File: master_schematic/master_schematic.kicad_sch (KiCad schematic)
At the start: 5 parts, among them U1 teensy_4.1

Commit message: added footprint library and a pcb file
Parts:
- removed U2: ~, symbol hb_symbol_lib:load_cell_yzc516_50kg
- added U3: ~, symbol hb_symbol_lib:new_load_cell_gx-1
- PT1: footprint (none) -> hb_footprint_lib:Pressure Transducer (Low)
- RM1: footprint (none) -> hb_footprint_lib:Radio_Module
- U1: footprint DEV-16771:MODULE_DEV-16771 -> hb_footprint_lib:teensy4.1
- U4: footprint (none) -> Connector_PinHeader_1.00mm:PinHeader_1x06_P1.00mm_Vertical
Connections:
- net LC_SIG+: now also U4.9 (A+), U3.2 (SIG+)
- net LC_SIG-: now also U4.8 (A-), U3.3 (SIG-)
- net LC_VDD: now reaches U4.12 (E+)
- net LC_VDD: now also U3.1 (VDD)
- net LC_GND: now reaches U4.7 (E-)
- net LC_GND: now also U3.4 (GND)
- net PT_INPUT renamed PT_OUTPUT
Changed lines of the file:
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@@
+	(wire
+		(pts
+			(xy 45.72 123.19) (xy 45.72 125.73)
+		)
+		(stroke
+			(width 0)
+			(type default)
+		)
+	)
 	(wire
 		(pts
@@
 	(wire
 		(pts
+			(xy 48.26 99.06) (xy 53.34 99.06)
+		)
+		(stroke
+			(width 0)
+			(type default)
+		)
+	)
+	(wire
+		(pts
 			(xy 168.91 73.66) (xy 175.26 73.66)
 		)
@@
 	(wire
 		(pts
+			(xy 50.8 123.19) (xy 50.8 125.73)
+		)
+		(stroke
+			(width 0)
+			(type default)
+		)
+	)
+	(wire
+		(pts
 			(xy 128.27 46.99) (xy 137.16 46.99)
 		)
@@
 	(wire
 		(pts
-			(xy 48.26 86.36) (xy 53.34 86.36)
+			(xy 48.26 123.19) (xy 48.26 125.73)
 		)
 		(stroke
@@
 	(wire
 		(pts
+			(xy 48.26 104.14) (xy 53.34 104.14)
+		)
+		(stroke
+			(width 0)
+			(type default)
+		)
+	)
+	(wire
+		(pts
 			(xy 80.01 82.55) (xy 87.63 82.55)
 		)
@@
 	(wire
 		(pts
-			(xy 48.26 88.9) (xy 53.34 88.9)
-		)
-		(stroke
-			(width 0)
-			(type default)
-		)
-	)
-	(wire
-		(pts
 			(xy 168.91 55.88) (xy 175.26 55.88)
 		)
@@
 	(wire
 		(pts
+			(xy 48.26 106.68) (xy 53.34 106.68)
+		)
+		(stroke
+			(width 0)
+			(type default)
+		)
+	)
+	(wire
+		(pts
 			(xy 168.91 71.12) (xy 175.26 71.12)
 		)
@@
 	(wire
 		(pts
+			(xy 58.42 123.19) (xy 58.42 125.73)
+		)
+		(stroke
+			(width 0)
+			(type default)
+		)
+	)
+	(wire
+		(pts
 			(xy 45.72 151.13) (xy 45.72 157.48)
 		)
@@
 	(wire
 		(pts
-			(xy 48.26 78.74) (xy 53.34 78.74)
-		)
-		(stroke
-			(width 0)
-			(type default)
-		)
-	)
-	(wire
-		(pts
 			(xy 128.27 140.97) (xy 135.89 140.97)
 		)
@@
 	(wire
 		(pts
-			(xy 48.26 81.28) (xy 53.34 81.28)
-		)
-		(stroke
-			(width 0)
-			(type default)
-		)
-	)
-	(wire
-		(pts
 			(xy 55.88 151.13) (xy 55.88 157.48)
 		)
@@
 		)
 	)
-	(label "LC_SIG+"
-		(at 53.34 81.28 0)
+	(wire
+		(pts
+			(xy 48.26 101.6) (xy 53.34 101.6)
+		)
+		(stroke
+			(width 0)
+			(type default)
+		)
+	)
+	(label "LC_SIG-"
+		(at 53.34 104.14 0)
 		(fields_autoplaced yes)
 		(effects
@@
 		)
 	)
+	(label "LC_SIG+"
+		(at 53.34 101.6 0)
+		(fields_autoplaced yes)
+		(effects
+			(font
+				(size 1.27 1.27)
+			)
+			(justify left bottom)
+		)
+	)
 	(label "AMP_DATA"
 		(at 55.88 157.48 270)
@@
 		)
 	)
+	(label "LC_SIG+"
+		(at 50.8 123.19 90)
+		(fields_autoplaced yes)
+		(effects
+			(font
+				(size 1.27 1.27)
+			)
+			(justify left bottom)
+		)
+	)
 	(label "CS4RM"
 		(at 168.91 73.66 180)
@@
 		)
 	)
-	(label "GND"
-		(at 53.34 88.9 0)
-		(fields_autoplaced yes)
-		(effects
-			(font
-				(size 1.27 1.27)
-			)
-			(justify left bottom)
-		)
-	)
-	(label "PT_INPUT"
+	(label "LC_GND"
+		(at 45.72 123.19 90)
+		(fields_autoplaced yes)
+		(effects
+			(font
+				(size 1.27 1.27)
+			)
+			(justify left bottom)
+		)
+	)
+	(label "PT_OUTPUT"
 		(at 80.01 115.57 180)
 		(fields_autoplaced yes)
@@
 			)
 			(justify right bottom)
-		)
-	)
-	(label "LC_SIG-"
-		(at 53.34 86.36 0)
-		(fields_autoplaced yes)
-		(effects
-			(font
-				(size 1.27 1.27)
-			)
-			(justify left bottom)
 		)
 	)
@@
 		)
 	)
+	(label "LC_VDD"
+		(at 58.42 123.19 90)
+		(fields_autoplaced yes)
+		(effects
+			(font
+				(size 1.27 1.27)
+			)
+			(justify left bottom)
+		)
+	)
 	(label "GND"
 		(at 168.91 58.42 180)
@@
 		)
 	)
+	(label "LC_VDD"
+		(at 53.34 99.06 0)
+		(fields_autoplaced yes)
+		(effects
+			(font
+				(size 1.27 1.27)
+			)
+			(justify left bottom)
+		)
+	)
 	(label "SCK"
 		(at 168.91 66.04 180)
@@
 		)
 	)
-	(label "5V"
-		(at 53.34 78.74 0)
-		(fields_autoplaced yes)
-		(effects
-			(font
-				(size 1.27 1.27)
-			)
-			(justify left bottom)
-		)
-	)
 	(label "RST4RM"
 		(at 168.91 76.2 180)
@@
 		)
 	)
+	(label "LC_GND"
+		(at 53.34 106.68 0)
+		(fields_autoplaced yes)
+		(effects
+			(font
+				(size 1.27 1.27)
+			)
+			(justify left bottom)
+		)
+	)
 	(label "IRQ4RM"
 		(at 80.01 74.93 180)
@@
 		)
 	)
-	(label "PT_INPUT"
+	(label "PT_OUTPUT"
 		(at 198.12 99.06 0)
+		(fields_autoplaced yes)
+		(effects
+			(font
+				(size 1.27 1.27)
+			)
+			(justify left bottom)
+		)
+	)
+	(label "LC_SIG-"
+		(at 48.26 123.19 90)
 		(fields_autoplaced yes)
 		(effects
@@
 			)
 		)
-		(property "Footprint" "DEV-16771:MODULE_DEV-16771"
+		(property "Footprint" "hb_footprint_lib:teensy4.1"
 			(at 108.458 163.576 0)
 			(effects
@@
 				(path "/c4f7e98c-e88d-49cc-9841-b70710a90a72"
 					(reference "U1")
+					(unit 1)
+				)
+			)
+		)
+	)
+	(symbol
+		(lib_id "hb_symbol_lib:new_load_cell_gx-1")
+		(at 40.64 102.87 0)
+		(unit 1)
+		(exclude_from_sim no)
+		(in_bom yes)
+		(on_board yes)
+		(dnp no)
+		(fields_autoplaced yes)
+		(property "Reference" "U3"
+			(at 40.005 93.98 0)
+			(effects
+				(font
+					(size 1.27 1.27)
+				)
+			)
+		)
+		(property "Value" "~"
+			(at 40.005 96.52 0)
+			(effects
+				(font
+					(size 1.27 1.27)
+				)
+			)
+		)
+		(property "Footprint" ""
+			(at 38.1 102.616 0)
+			(effects
+				(font
+					(size 1.27 1.27)
+				)
+				(hide yes)
+			)
+		)
+		(property "Datasheet" ""
+			(at 38.1 102.616 0)
+			(effects
+				(font
+					(size 1.27 1.27)
+				)
+				(hide yes)
+			)
+		)
+		(property "Description" ""
+			(at 38.1 102.616 0)
+			(effects
+				(font
+					(size 1.27 1.27)
+				)
+				(hide yes)
+			)
+		)
+		(pin "1"
+		)
+		(pin "2"
+		)
+		(pin "3"
+		)
+		(pin "4"
+		)
+		(instances
+			(project ""
+				(path "/c4f7e98c-e88d-49cc-9841-b70710a90a72"
+					(reference "U3")
 					(unit 1)
 				)
@@
 			)
 		)
-		(property "Footprint" ""
+		(property "Footprint" "hb_footprint_lib:Radio_Module"
 			(at 195.58 52.07 0)
 			(effects
@@
 			)
 		)
-		(property "Footprint" ""
+		(property "Footprint" "hb_footprint_lib:Pressure Transducer (Low)"
 			(at 184.15 101.6 0)
 			(effects
@@
 				(path "/c4f7e98c-e88d-49cc-9841-b70710a90a72"
 					(reference "PT1")
-					(unit 1)
-				)
-			)
-		)
-	)
-	(symbol
-		(lib_id "hb_symbol_lib:load_cell_yzc516_50kg")
-		(at 38.1 82.55 0)
-		(unit 1)
-		(exclude_from_sim no)
-		(in_bom yes)
-		(on_board yes)
-		(dnp no)
-		(fields_autoplaced yes)
-		(property "Reference" "U2"
-			(at 38.735 73.66 0)
-			(effects
-				(font
-					(size 1.27 1.27)
-				)
-			)
-		)
-		(property "Value" "~"
-			(at 38.735 76.2 0)
-			(effects
-				(font
-					(size 1.27 1.27)
-				)
-			)
-		)
-		(property "Footprint" ""
-			(at 38.1 82.55 0)
-			(effects
-				(font
-					(size 1.27 1.27)
-				)
-				(hide yes)
-			)
-		)
-		(property "Datasheet" ""
-			(at 38.1 82.55 0)
-			(effects
-				(font
-					(size 1.27 1.27)
-				)
-				(hide yes)
-			)
-		)
-		(property "Description" ""
-			(at 38.1 82.55 0)
-			(effects
-				(font
-					(size 1.27 1.27)
-				)
-				(hide yes)
-			)
-		)
-		(pin "5"
-		)
-		(pin "1"
-		)
-		(pin "3"
-		)
-		(pin "4"
-		)
-		(pin "2"
-		)
-		(instances
-			(project ""
-				(path "/c4f7e98c-e88d-49cc-9841-b70710a90a72"
-					(reference "U2")
 					(unit 1)
 				)
@@
 			)
 		)
-		(property "Footprint" ""
+		(property "Footprint" "Connector_PinHeader_1.00mm:PinHeader_1x06_P1.00mm_Vertical"
 			(at 52.07 138.176 0)
 			(effects

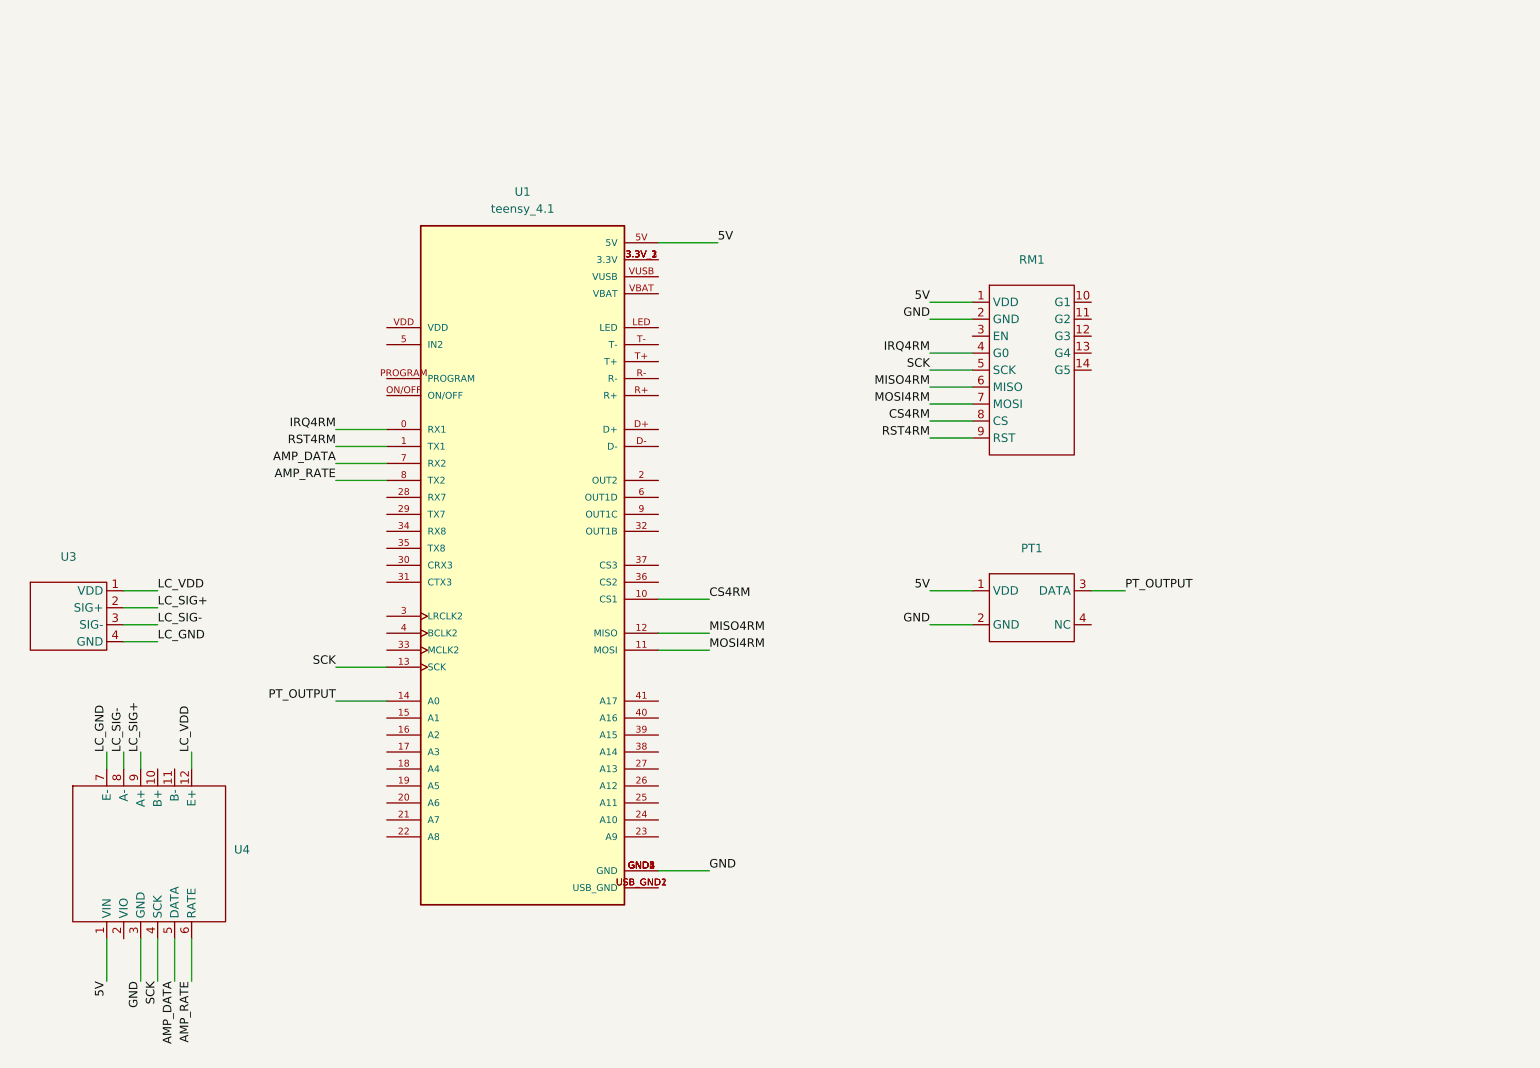
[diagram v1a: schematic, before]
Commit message: Added symbol libraries for HX711 and the transistor IRLZ34NPBF. Made schematic for solenoid valve.
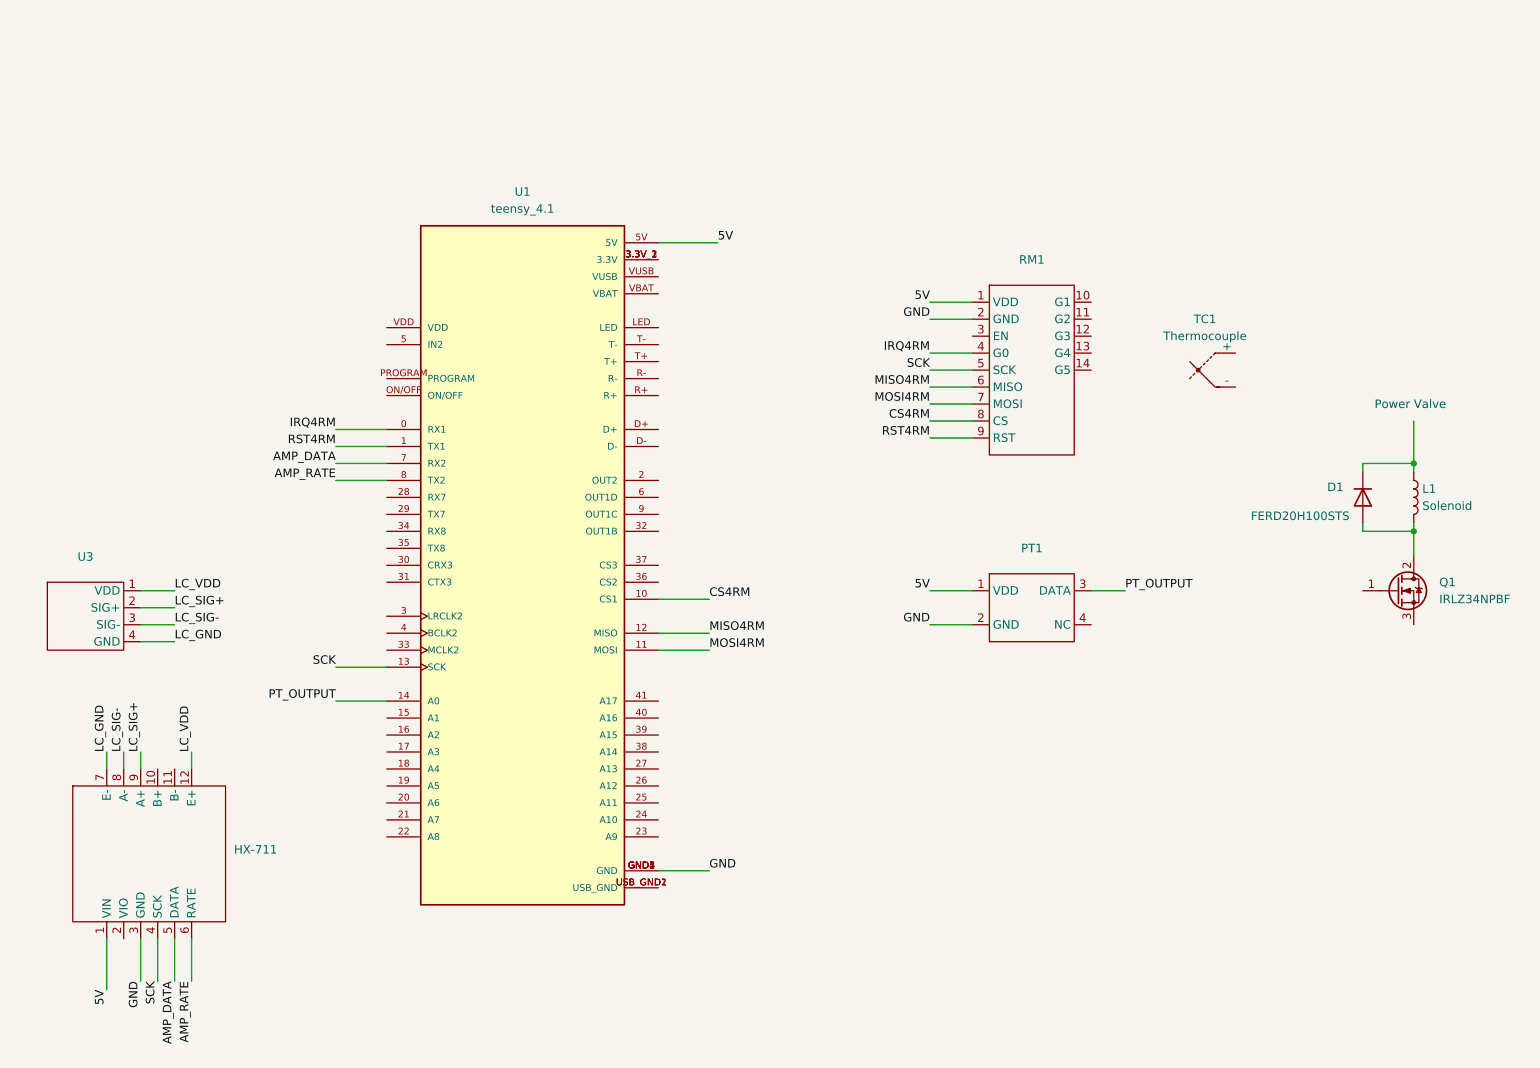
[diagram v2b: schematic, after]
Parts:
- added D1: FERD20H100STS, symbol Device:D
- added L1: Solenoid, symbol Device:L
- added Q1: IRLZ34NPBF, IRLZ34NPBF:TO-220AB_INF, symbol Transistor_FET:IRLZ34N
- added TC1: Thermocouple, symbol Device:Thermocouple
- renumbered U4 to HX-711
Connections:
- new net: D1.1 (K), L1.1
- new net: D1.2 (A), L1.2, Q1.2 (D)
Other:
- note added: "Power Valve"
- moved on the sheet: U3

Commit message: added sheet and connections for PT
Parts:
- removed PT1: ~, hb_footprint_lib:Pressure Transducer (Low), symbol hb_symbol_lib:pressure_transducer
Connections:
- net PT1_N: now reaches U1.15 (A1)
- net PT2_N: now reaches U1.16 (A2)
- net PT1_P: now reaches U1.17 (A3)
- net PT1_T: now reaches U1.18 (A4)
- net PT1_I: now reaches U1.19 (A5)
- net PT2_I: now reaches U1.20 (A6)
- net PT3_I: now reaches U1.21 (A7)
- net PT4_I: now reaches U1.22 (A8)
- net PT5_I: now reaches U1.23 (A9)
- net 5V renamed +5V
- net PT_OUTPUT renamed PT1_O
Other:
- added sheet pressure_transducers (pts.kicad_sch)
- moved on the sheet: D1, L1, Q1, RM1, TC1, U1
